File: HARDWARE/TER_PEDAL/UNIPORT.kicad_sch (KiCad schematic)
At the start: 1 part, among them J3 RJ45_Shielded

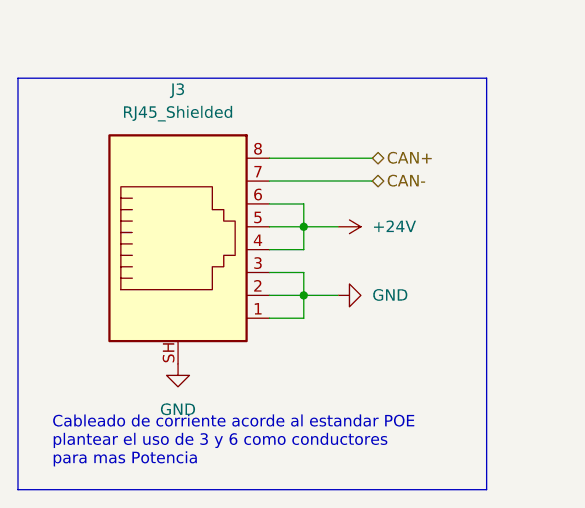
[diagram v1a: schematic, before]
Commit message: The RJ45 pinout was incorrect according to the poe standard, started redesign and relocation of the board revision
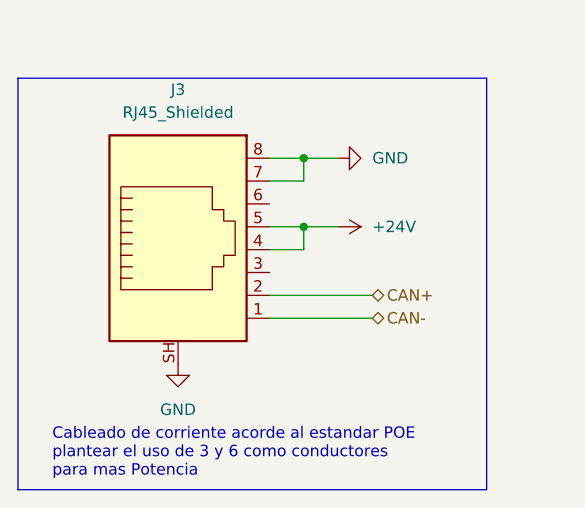
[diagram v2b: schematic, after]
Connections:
- net +24V: no longer J3.6
- net CAN+: now also J3.2; no longer J3.8
- net CAN-: now also J3.1; no longer J3.7
- net GND: now also J3.7, J3.8; no longer J3.1, J3.2, J3.3
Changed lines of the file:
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@@
 (kicad_sch (version 20230121) (generator eeschema)
   (paper "A4")
-  (junction (at 146.05 92.71) (diameter 0) (color 0 0 0 0)
+  (junction (at 146.05 77.47) (diameter 0) (color 0 0 0 0)
   )
   (junction (at 146.05 85.09) (diameter 0) (color 0 0 0 0)
   )
-  (wire (pts (xy 146.05 82.55) (xy 146.05 85.09))
-    (stroke (width 0) (type default))
-  )
-  (wire (pts (xy 142.24 80.01) (xy 153.67 80.01))
-    (stroke (width 0) (type default))
-  )
-  (wire (pts (xy 146.05 92.71) (xy 146.05 95.25))
-    (stroke (width 0) (type default))
-  )
-  (wire (pts (xy 142.24 90.17) (xy 146.05 90.17))
-    (stroke (width 0) (type default))
-  )
-  (wire (pts (xy 142.24 82.55) (xy 146.05 82.55))
+  (wire (pts (xy 142.24 95.25) (xy 153.67 95.25))
+    (stroke (width 0) (type default))
+  )
+  (wire (pts (xy 146.05 77.47) (xy 146.05 80.01))
     (stroke (width 0) (type default))
   )
@@
     (stroke (width 0) (type default))
   )
-  (wire (pts (xy 142.24 92.71) (xy 146.05 92.71))
+  (wire (pts (xy 142.24 80.01) (xy 146.05 80.01))
     (stroke (width 0) (type default))
   )
@@
     (stroke (width 0) (type default))
   )
-  (wire (pts (xy 142.24 95.25) (xy 146.05 95.25))
-    (stroke (width 0) (type default))
-  )
-  (wire (pts (xy 149.86 92.71) (xy 146.05 92.71))
+  (wire (pts (xy 142.24 77.47) (xy 146.05 77.47))
     (stroke (width 0) (type default))
   )
@@
     (stroke (width 0) (type default))
   )
-  (wire (pts (xy 142.24 77.47) (xy 153.67 77.47))
+  (wire (pts (xy 149.86 77.47) (xy 146.05 77.47))
     (stroke (width 0) (type default))
   )
@@
     (stroke (width 0) (type default))
   )
-  (wire (pts (xy 146.05 90.17) (xy 146.05 92.71))
+  (wire (pts (xy 142.24 92.71) (xy 153.67 92.71))
     (stroke (width 0) (type default))
   )
@@
   )
   (text "Cableado de corriente acorde al estandar POE\nplantear el uso de 3 y 6 como conductores\npara mas Potencia\n"
-    (at 118.11 111.76 0)
+    (at 118.11 113.03 0)
     (effects (font (size 1.27 1.27)) (justify left bottom))
   )
-  (hierarchical_label "CAN+" (shape bidirectional) (at 153.67 77.47 0) (fields_autoplaced)
+  (hierarchical_label "CAN+" (shape bidirectional) (at 153.67 92.71 0) (fields_autoplaced)
     (effects (font (size 1.27 1.27)) (justify left))
   )
-  (hierarchical_label "CAN-" (shape bidirectional) (at 153.67 80.01 0) (fields_autoplaced)
+  (hierarchical_label "CAN-" (shape bidirectional) (at 153.67 95.25 0) (fields_autoplaced)
     (effects (font (size 1.27 1.27)) (justify left))
   )
@@
         (path "/73ede3a3-6344-40fe-9207-10ff50d388ba/667e740b-7c5a-4284-8e8d-cd79a8a36981"
           (reference "#PWR0101") (unit 1)
+        )
+      )
+    )
+  )
+  (symbol (lib_id "power:GND") (at 149.86 77.47 90) (unit 1)
+    (in_bom yes) (on_board yes) (dnp no) (fields_autoplaced)
+    (property "Reference" "#PWR020" (at 156.21 77.47 0)
+      (effects (font (size 1.27 1.27)) hide)
+    )
+    (property "Value" "GND" (at 153.67 77.4699 90)
+      (effects (font (size 1.27 1.27)) (justify right))
+    )
+    (property "Footprint" "" (at 149.86 77.47 0)
+      (effects (font (size 1.27 1.27)) hide)
+    )
+    (property "Datasheet" "" (at 149.86 77.47 0)
+      (effects (font (size 1.27 1.27)) hide)
+    )
+    (pin "1")
+    (instances
+      (project "TER_MAIN_MODULE"
+        (path "/4d50337d-0f48-4e70-bc68-0638d7f1b220/6e820524-bbb2-4b9e-897e-5491d1a946cc"
+          (reference "#PWR020") (unit 1)
+        )
+        (path "/4d50337d-0f48-4e70-bc68-0638d7f1b220/3be90758-2bc9-4709-b067-2e2824c6939d"
+          (reference "#PWR026") (unit 1)
+        )
+        (path "/4d50337d-0f48-4e70-bc68-0638d7f1b220/a976900c-90fd-4a1c-9099-675c63c76c34"
+          (reference "#PWR029") (unit 1)
+        )
+        (path "/4d50337d-0f48-4e70-bc68-0638d7f1b220/6098c490-bd23-4392-ad14-da81e33f66be"
+          (reference "#PWR032") (unit 1)
+        )
+        (path "/4d50337d-0f48-4e70-bc68-0638d7f1b220/c2684b12-c9fc-4671-b465-93b61dafa44a"
+          (reference "#PWR023") (unit 1)
+        )
+      )
+      (project "TER_PEDAL"
+        (path "/73ede3a3-6344-40fe-9207-10ff50d388ba/667e740b-7c5a-4284-8e8d-cd79a8a36981"
+          (reference "#PWR048") (unit 1)
         )
       )
@@
         )
       )
-    )
-  )
-  (symbol (lib_id "power:GND") (at 149.86 92.71 90) (unit 1)
-    (in_bom yes) (on_board yes) (dnp no) (fields_autoplaced)
-    (property "Reference" "#PWR020" (at 156.21 92.71 0)
-      (effects (font (size 1.27 1.27)) hide)
-    )
-    (property "Value" "GND" (at 153.67 92.7099 90)
-      (effects (font (size 1.27 1.27)) (justify right))
-    )
-    (property "Footprint" "" (at 149.86 92.71 0)
-      (effects (font (size 1.27 1.27)) hide)
-    )
-    (property "Datasheet" "" (at 149.86 92.71 0)
-      (effects (font (size 1.27 1.27)) hide)
-    )
-    (pin "1")
-    (instances
-      (project "TER_MAIN_MODULE"
-        (path "/4d50337d-0f48-4e70-bc68-0638d7f1b220/6e820524-bbb2-4b9e-897e-5491d1a946cc"
-          (reference "#PWR020") (unit 1)
-        )
-        (path "/4d50337d-0f48-4e70-bc68-0638d7f1b220/3be90758-2bc9-4709-b067-2e2824c6939d"
-          (reference "#PWR026") (unit 1)
-        )
-        (path "/4d50337d-0f48-4e70-bc68-0638d7f1b220/a976900c-90fd-4a1c-9099-675c63c76c34"
-          (reference "#PWR029") (unit 1)
-        )
-        (path "/4d50337d-0f48-4e70-bc68-0638d7f1b220/6098c490-bd23-4392-ad14-da81e33f66be"
-          (reference "#PWR032") (unit 1)
-        )
-        (path "/4d50337d-0f48-4e70-bc68-0638d7f1b220/c2684b12-c9fc-4671-b465-93b61dafa44a"
-          (reference "#PWR023") (unit 1)
-        )
-      )
-      (project "TER_PEDAL"
-        (path "/73ede3a3-6344-40fe-9207-10ff50d388ba/667e740b-7c5a-4284-8e8d-cd79a8a36981"
-          (reference "#PWR0102") (unit 1)
-        )
-      )

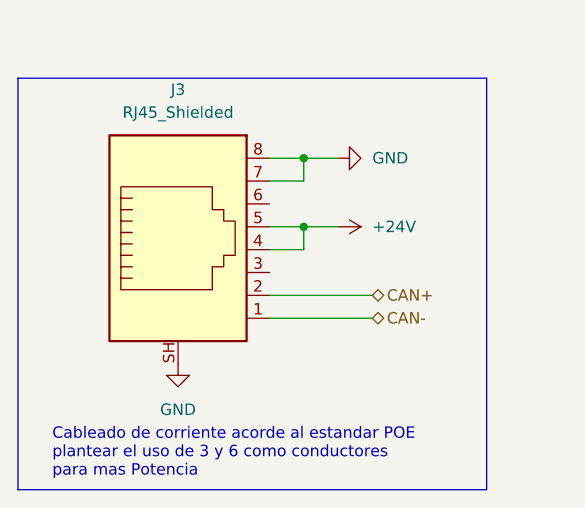
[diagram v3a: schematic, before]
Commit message: Added voltage followers to sensing, improved can circuitri, improved layout, waiting for routing
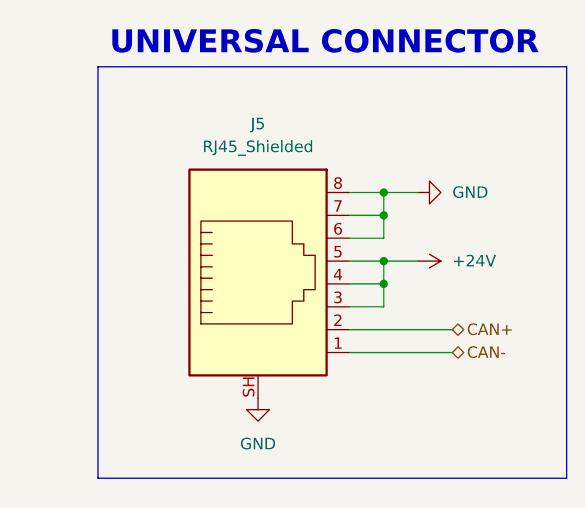
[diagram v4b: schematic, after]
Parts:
- renumbered J3 to J5
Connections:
- net +24V: now also J5.3
- net GND: now also J5.6
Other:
- note added: "UNIVERSAL CONNECTOR"
- note removed: "Cableado de corriente acorde al estandar POE plantear el uso de 3 y 6 como conductores para mas Potencia"
- company: (none) -> Tecnun-eRacing
- title: (none) -> TeR_PEDAL
- moved on the sheet: J5
